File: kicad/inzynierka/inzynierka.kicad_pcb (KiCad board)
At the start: 2 copper layers, 170 x 175 mm, 49 parts

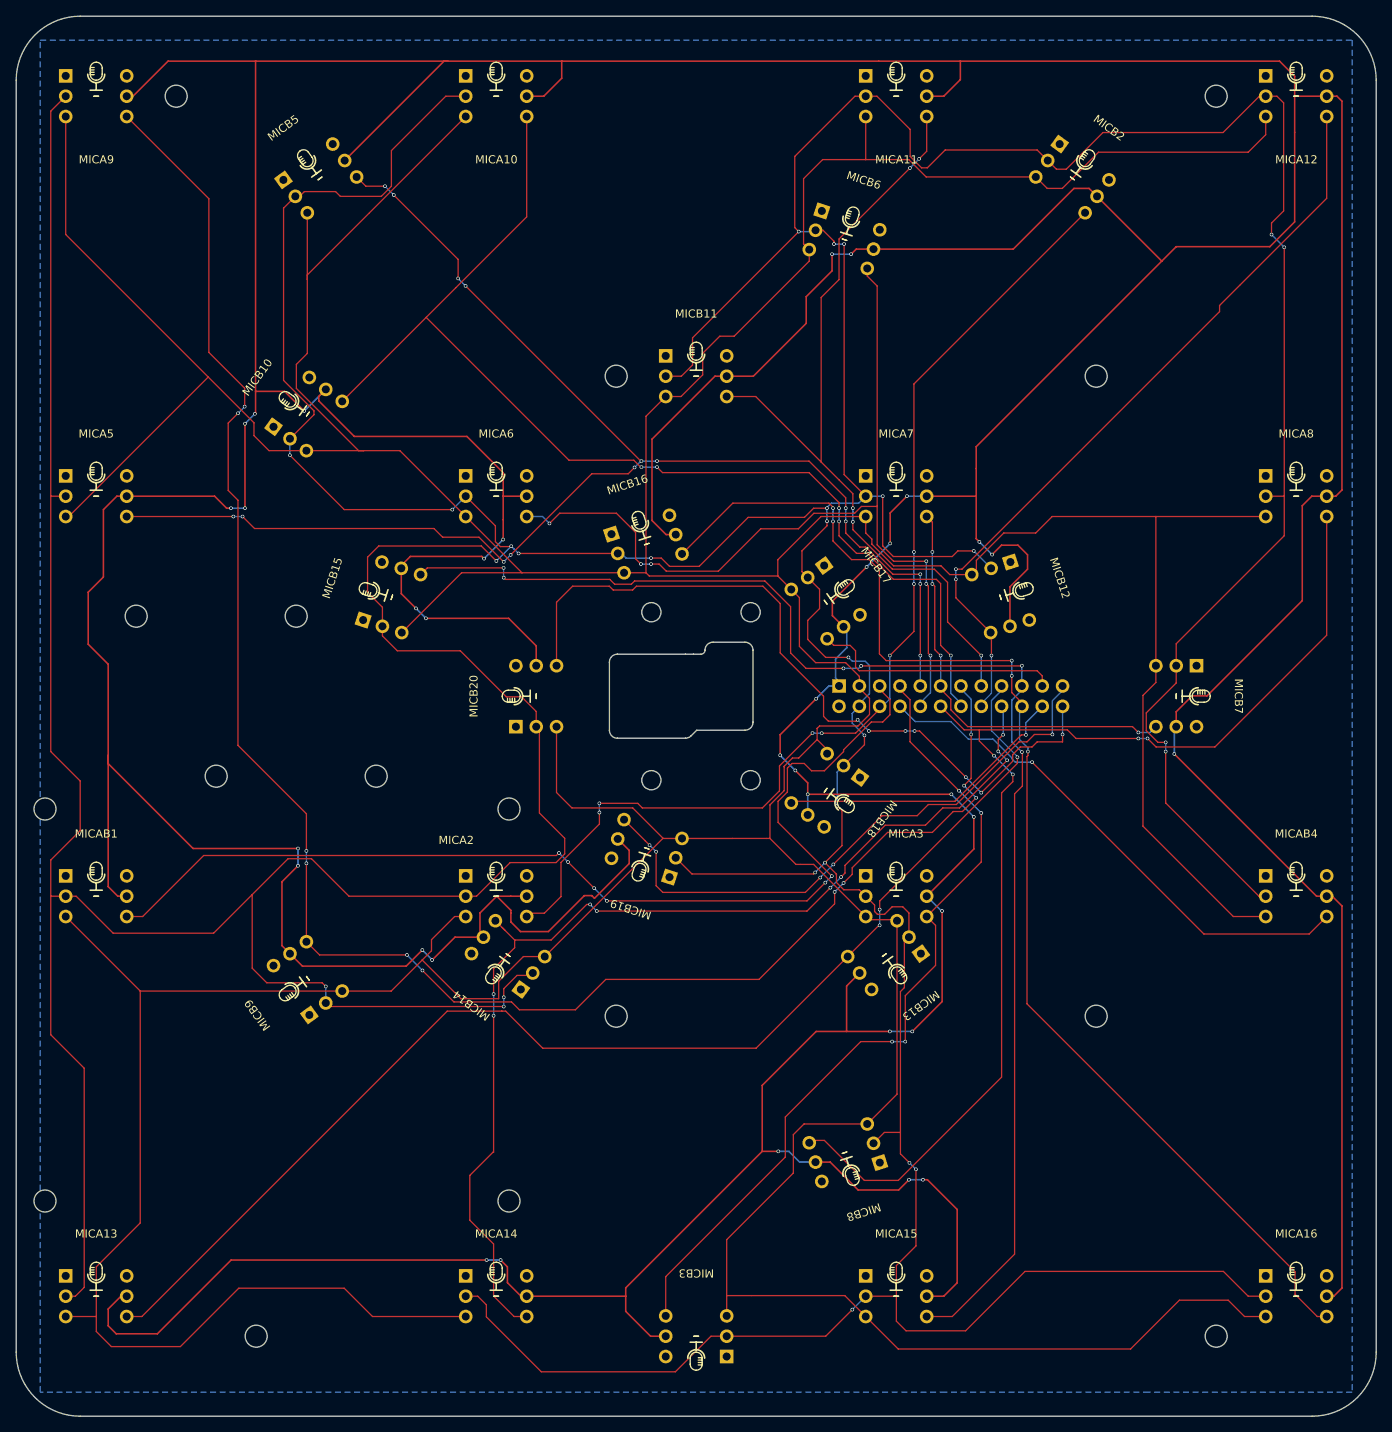
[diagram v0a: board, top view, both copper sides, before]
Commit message: Zwiększenie rozmiaru przelotek
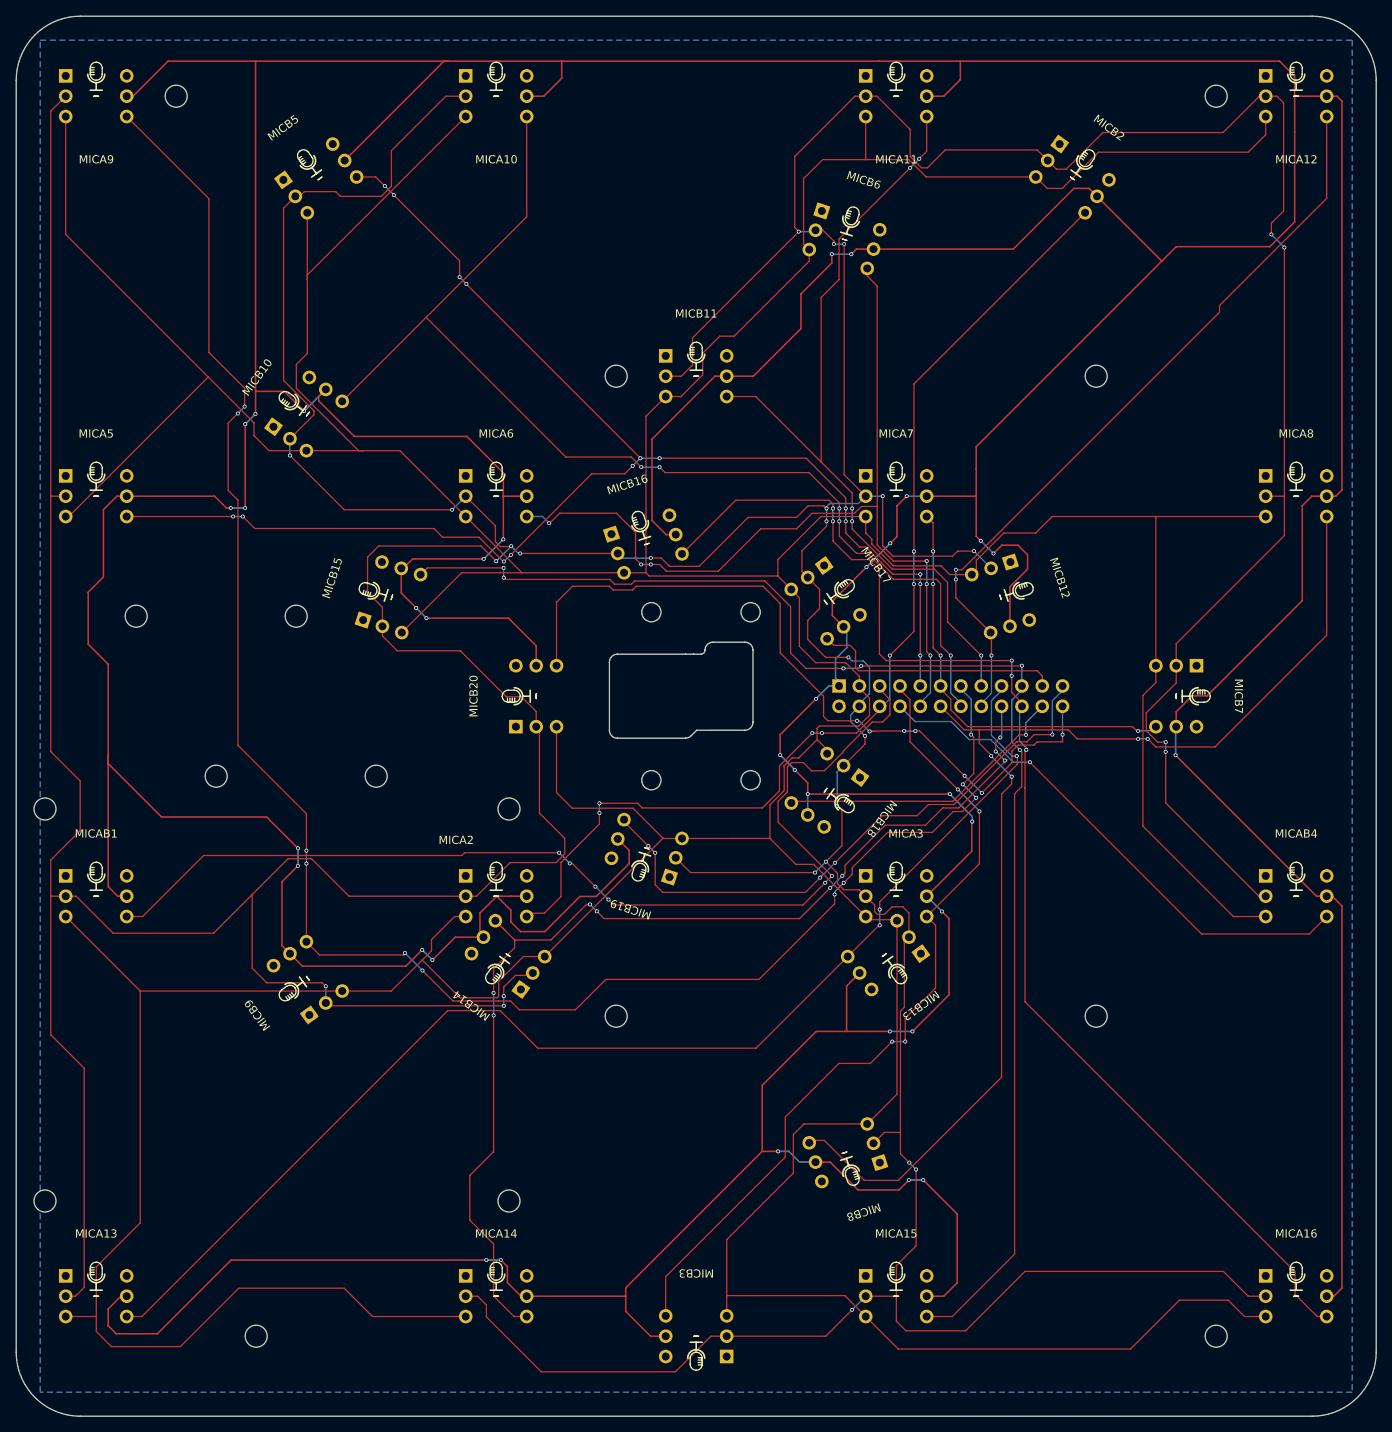
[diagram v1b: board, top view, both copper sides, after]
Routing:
- net D14: track 136.9 -> 138.0 mm
- net +3.3V: track 1185.1 -> 1184.1 mm
- net D9: track 229.2 -> 229.9 mm
- net D1: track 132.6 -> 133.1 mm
- net D16: track 160.2 -> 160.8 mm

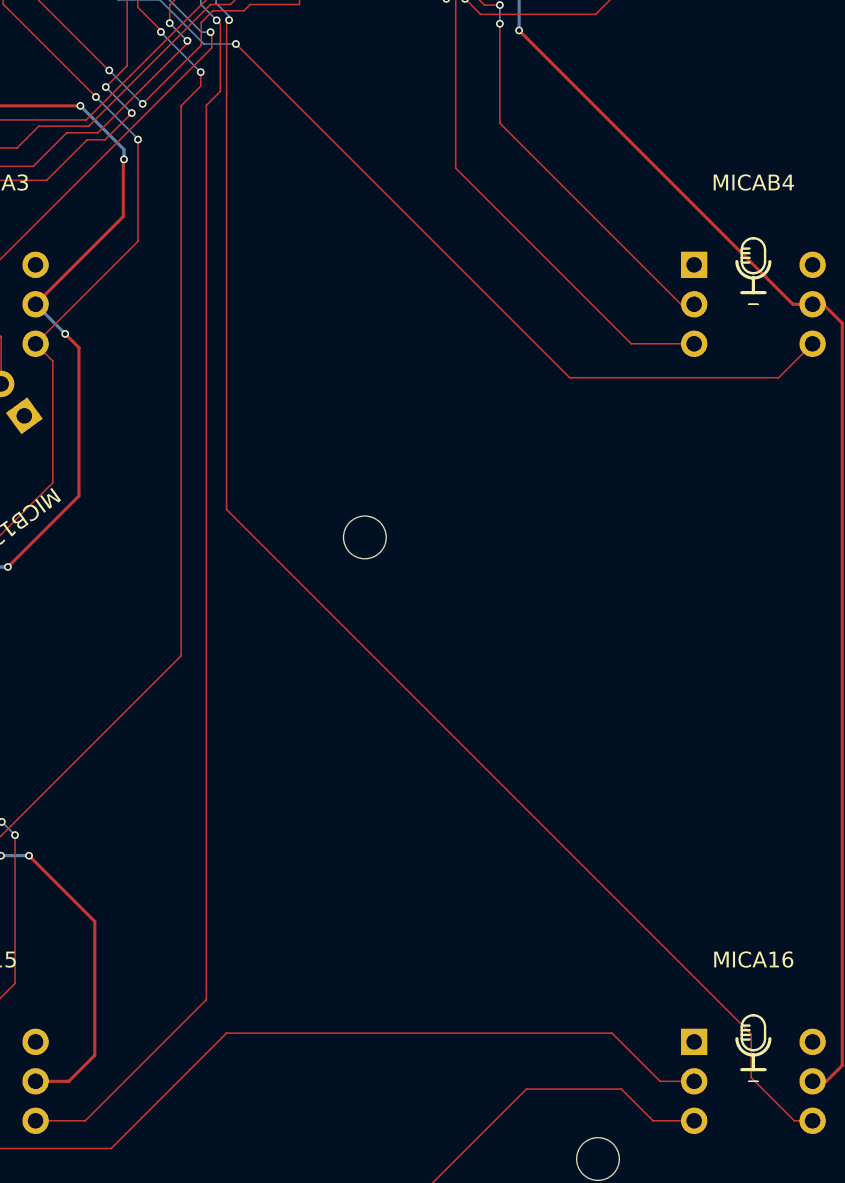
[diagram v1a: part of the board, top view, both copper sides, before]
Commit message: Dodanie padów testowych
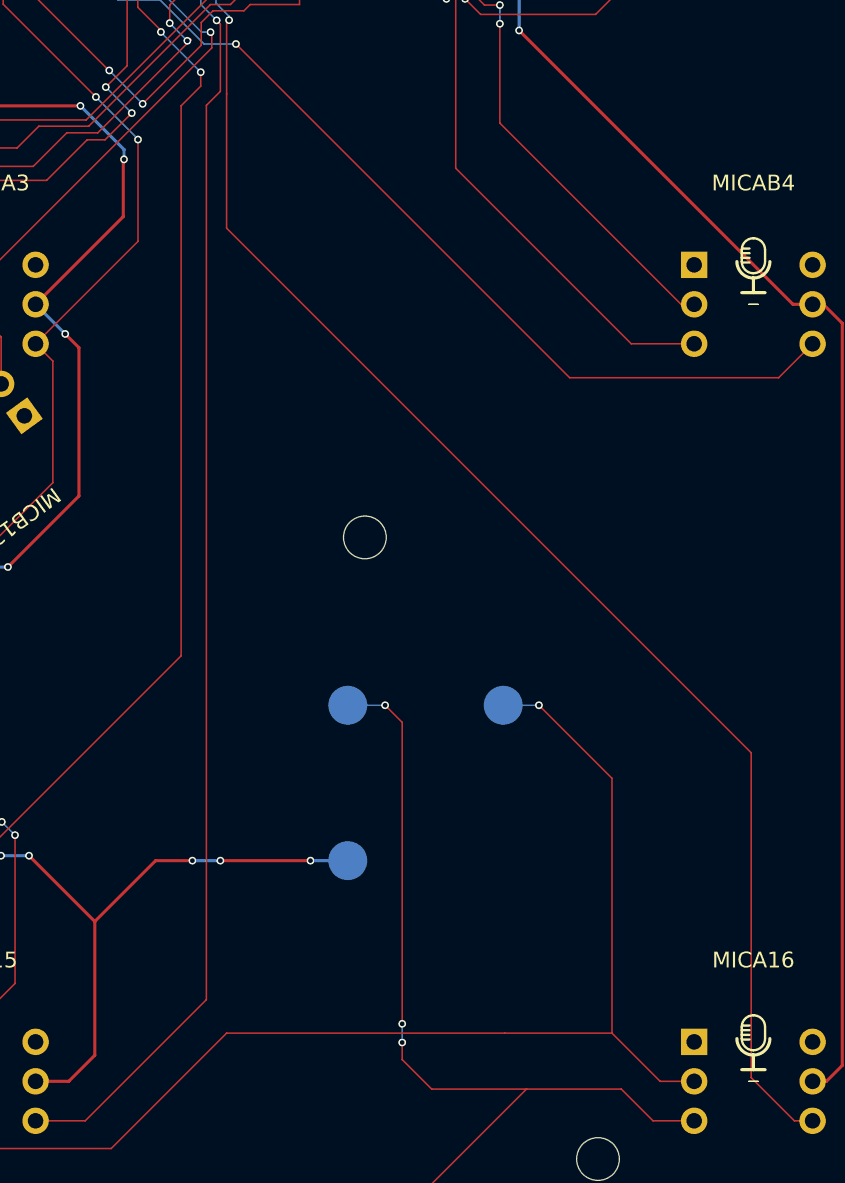
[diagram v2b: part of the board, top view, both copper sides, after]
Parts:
- added 3.3V: 3.3V, TestPoint:TestPoint_Pad_D2.5mm, B.Cu at (150.4, 160.8)
- added CLK1: CLK1, TestPoint:TestPoint_Pad_D2.5mm, B.Cu at (150.4, 150.8)
- added CLK2: CLK2, TestPoint:TestPoint_Pad_D2.5mm, B.Cu at (160.4, 150.8)
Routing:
- net CLK1: track 936.5 -> 970.9 mm, vias 0 -> 3
- net CLK2: track 1061.3 -> 1086.6 mm, vias 28 -> 29
- net +3.3V: track 1184.1 -> 1202.0 mm, vias 35 -> 38

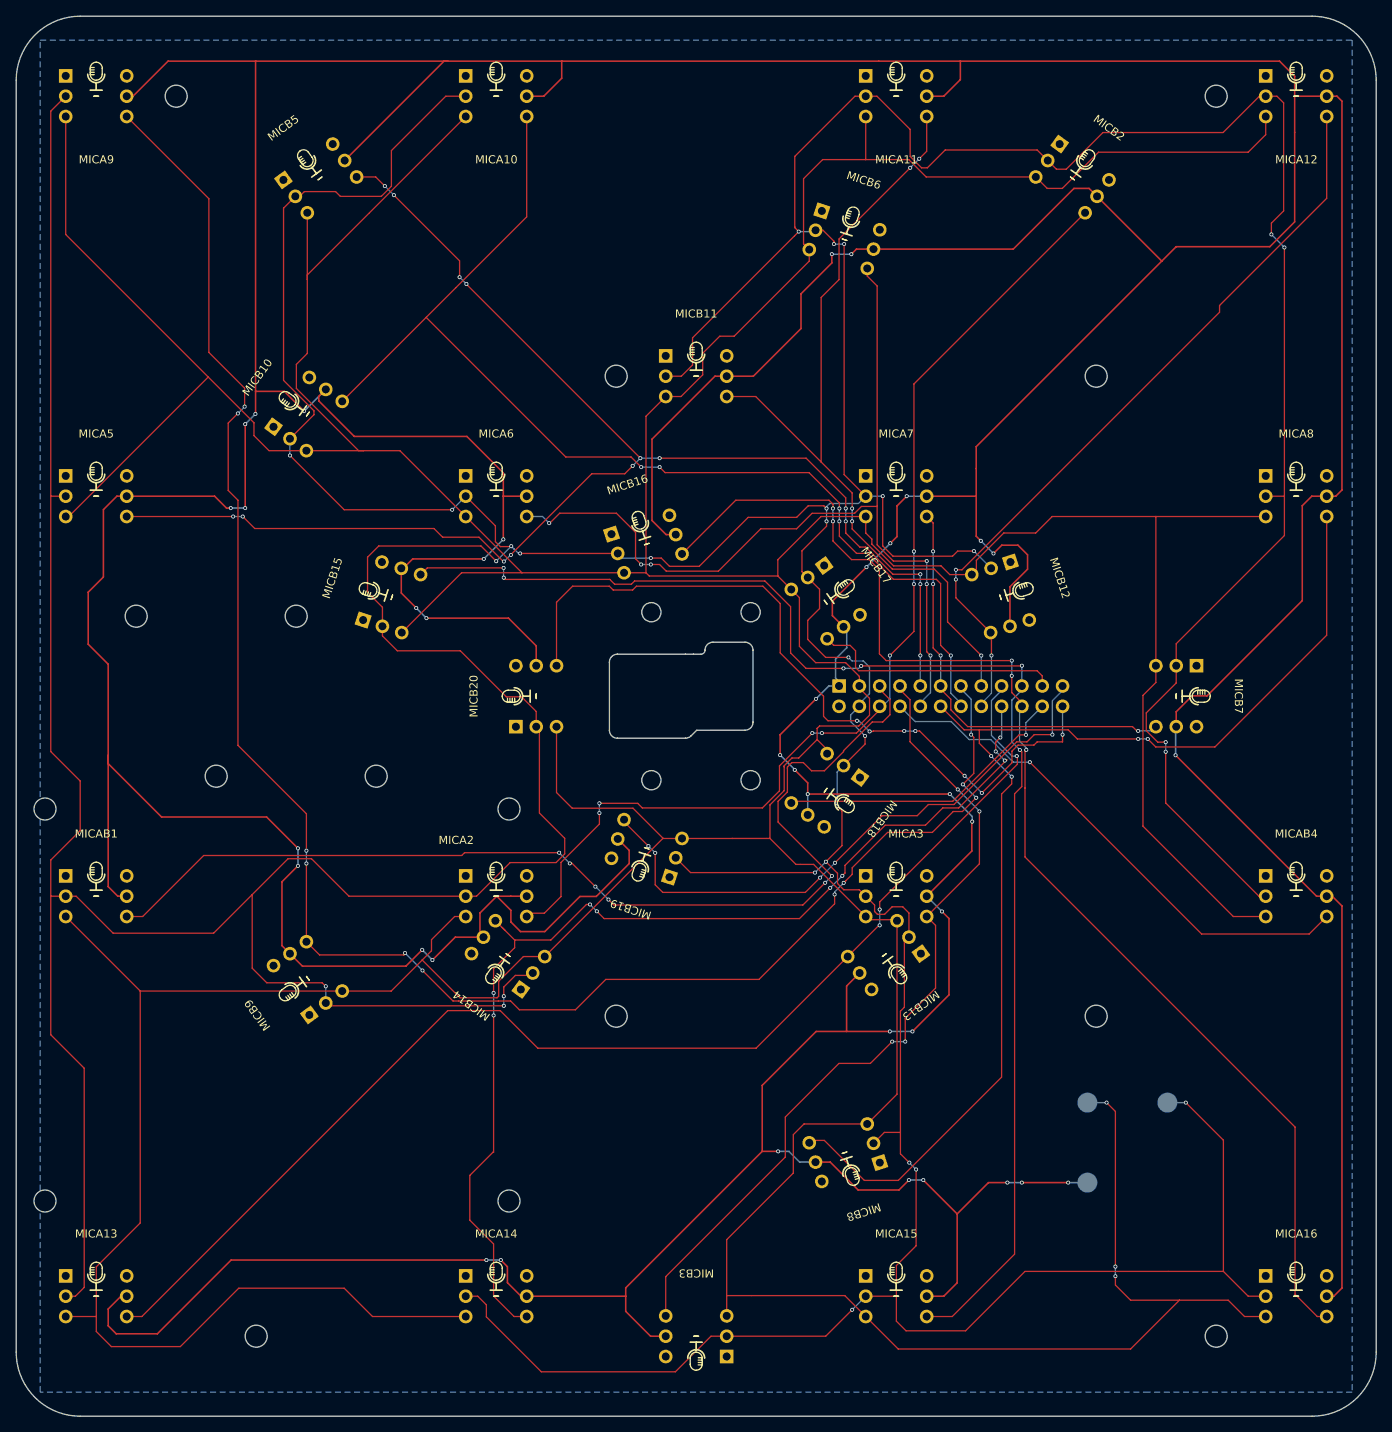
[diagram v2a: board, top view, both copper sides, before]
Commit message: Poszerzenie ścieżek do 0.14mm
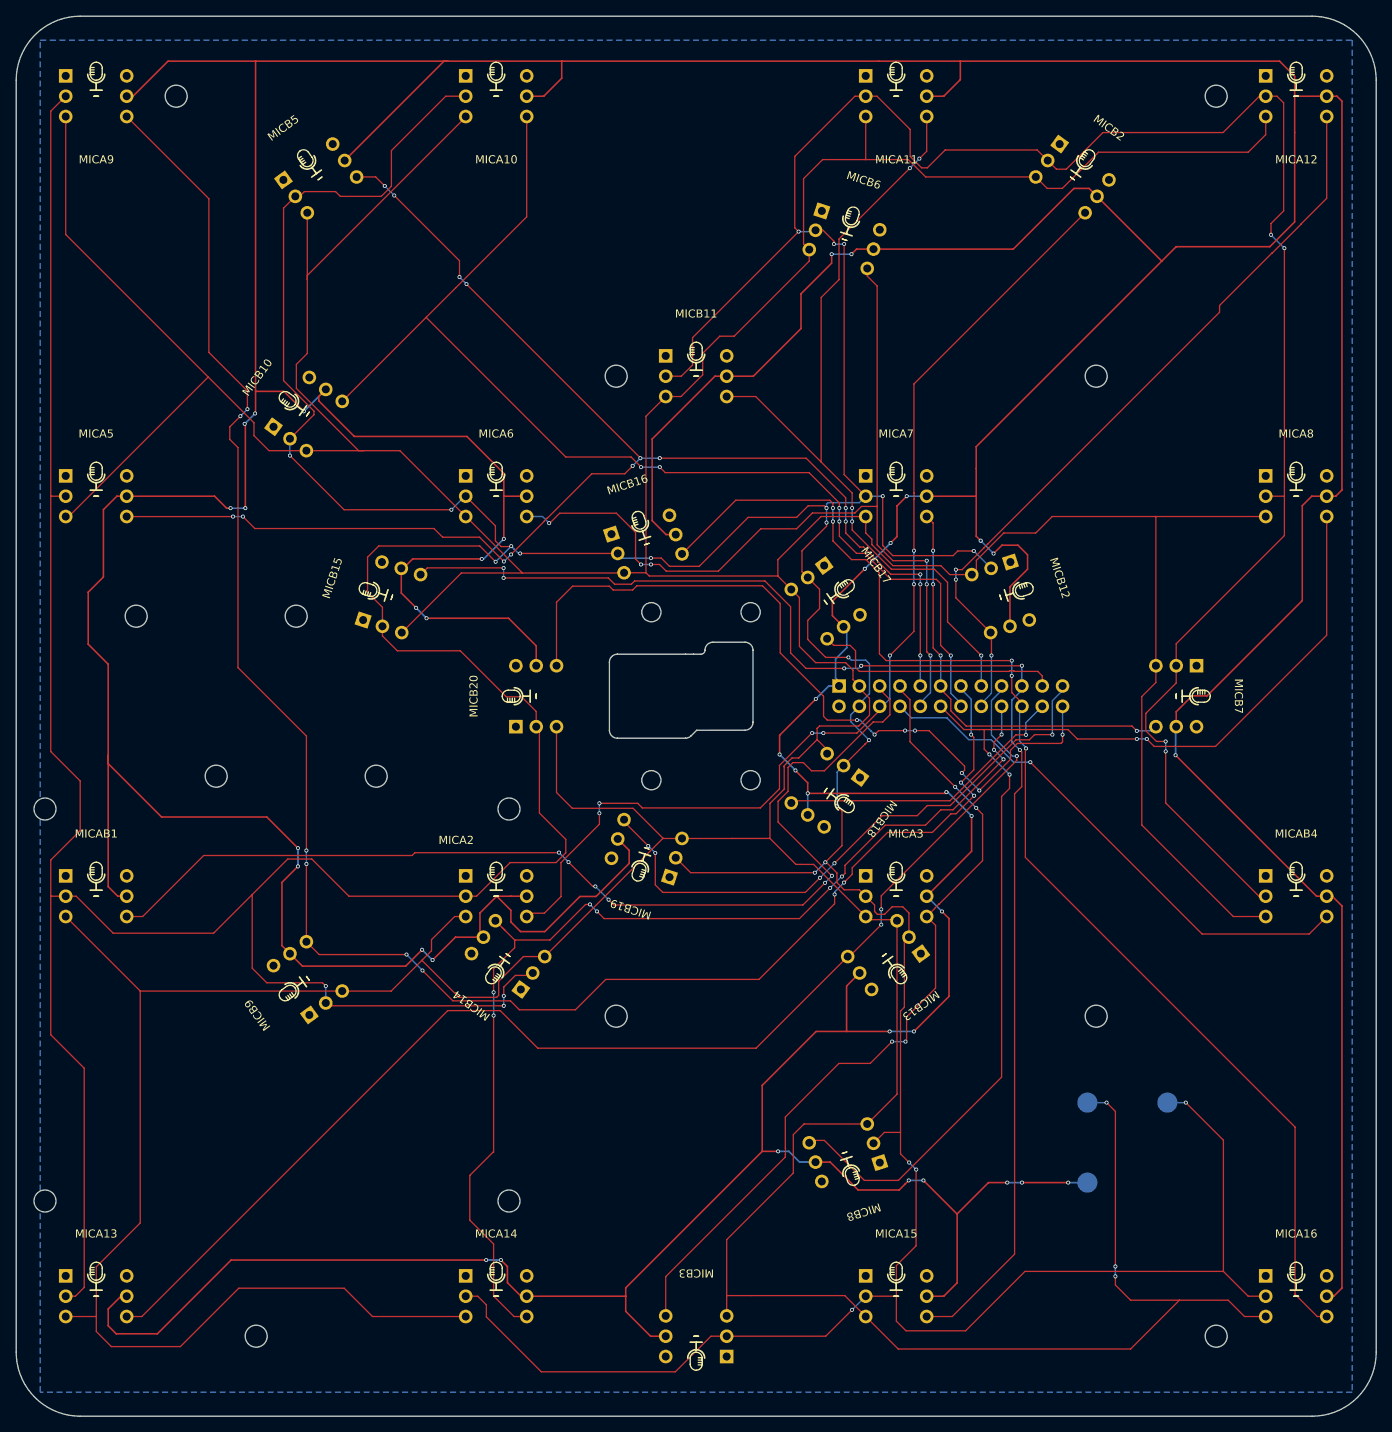
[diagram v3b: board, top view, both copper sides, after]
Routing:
- net CLK2: track 1086.6 -> 1087.6 mm
- net D20: track 96.2 -> 97.2 mm
- net D14: track 138.0 -> 137.3 mm
